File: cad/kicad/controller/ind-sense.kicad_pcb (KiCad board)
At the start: 2 copper layers, 32.5 x 81.2 mm, 21 parts, among them J1 Conn_01x27, J2 Conn_01x18, U1 74HC154, U2 MCP4821, U3 CMP04, U4 CMP04

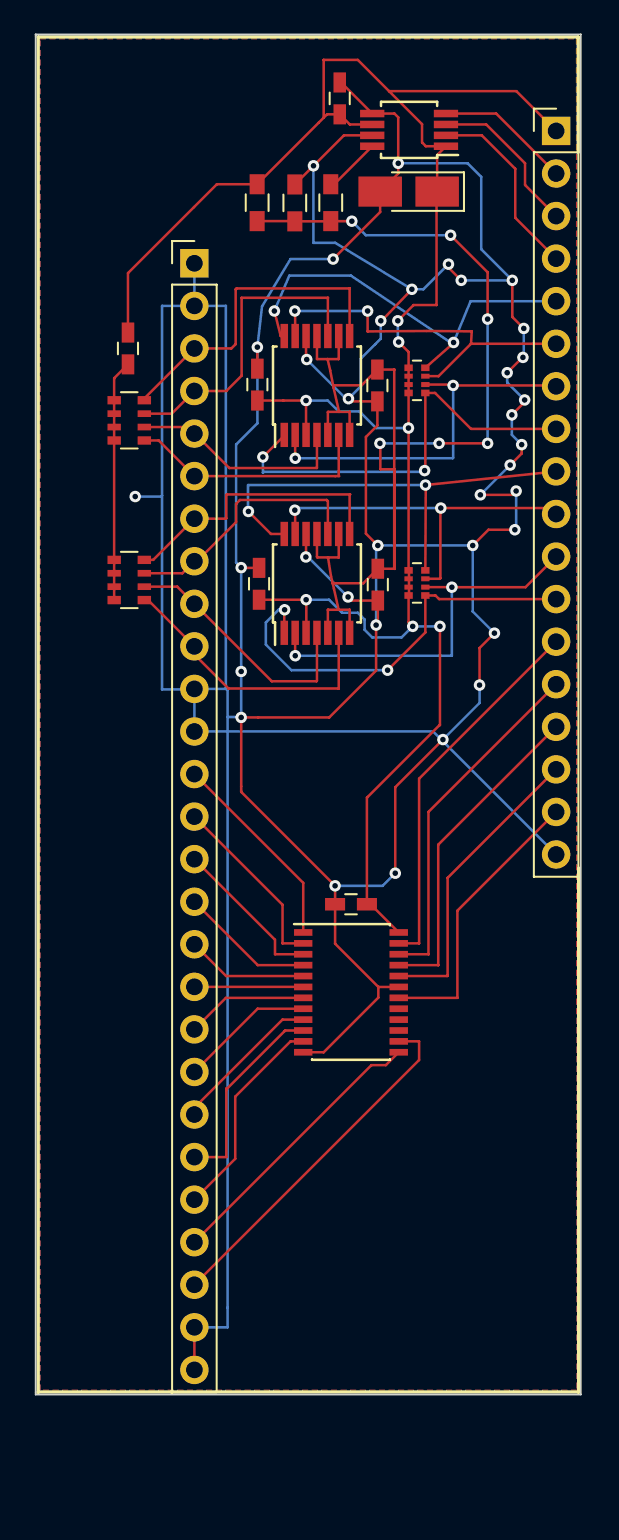
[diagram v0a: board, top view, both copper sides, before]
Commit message: updated controller with a lower part count equivalent, that should also be more accurate. need to have an actuall EE review the board and it's design
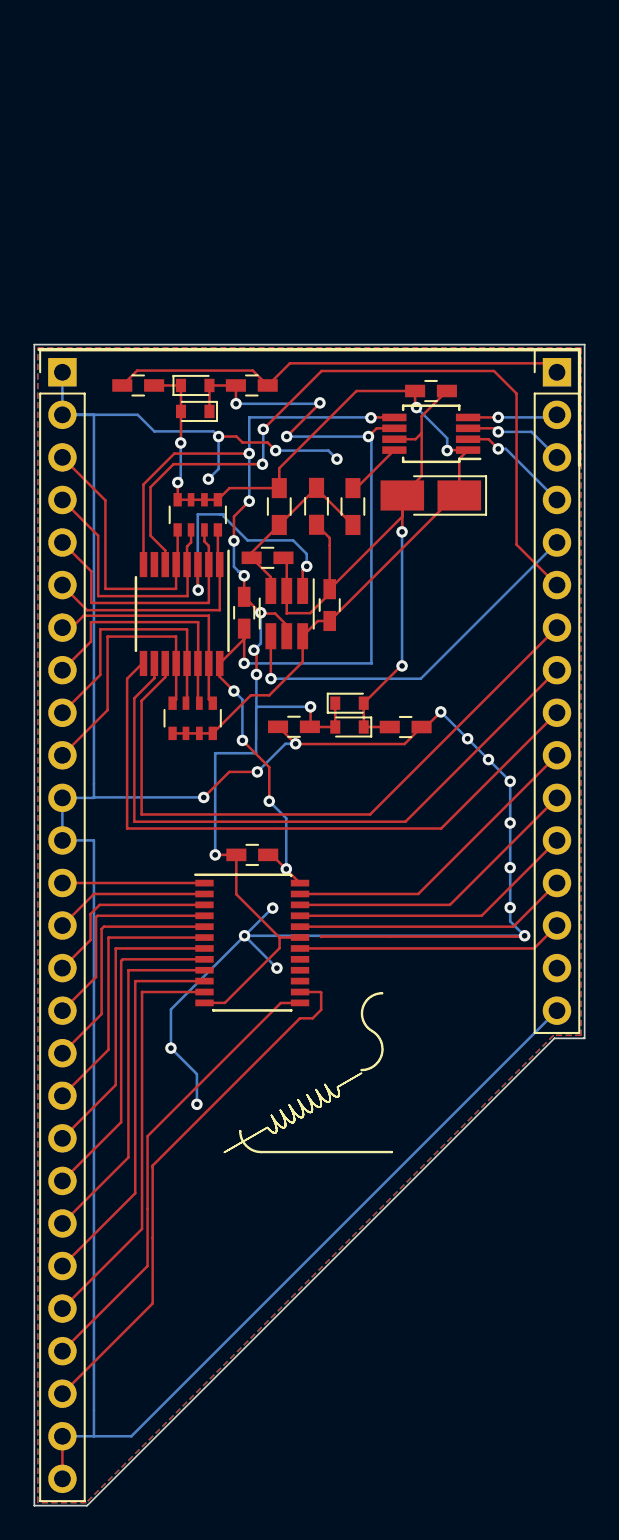
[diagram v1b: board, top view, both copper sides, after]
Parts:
- removed RN3, RN4: 66k, Resistors_SMD:R_Array_Convex_4x0402
- added C10: 0u1, Capacitors_SMD:C_0603_HandSoldering, F.Cu at (163.3, 56.5)
- added C9: 0u1, Capacitors_SMD:C_0603_HandSoldering, F.Cu at (156.6, 56.5)
- added D1: ~, Diodes_SMD:D_0603, F.Cu at (169.2, 76.8)
- added D2: ~, Diodes_SMD:D_0603, F.Cu at (169.2, 75.4)
- added D3: ~, Diodes_SMD:D_0603, F.Cu at (160.0, 56.5)
- added D4: ~, Diodes_SMD:D_0603, F.Cu at (160.0, 58.0)
- C2: value 100u -> 0u1
- J2: value Conn_01x18 -> Conn_01x16; footprint Pin_Headers:Pin_Header_Straight_1x18_Pitch2.54mm -> Pin_Headers:Pin_Header_Straight_1x16_Pitch2.54mm
- RN1, RN2: value 330 -> 2k64
- U3: value CMP04 -> NX3L4051; footprint Housings_SSOP:TSSOP-14_4.4x5mm_Pitch0.65mm -> Housings_SSOP:TSSOP-16_4.4x5mm_Pitch0.65mm
- U4: value CMP04 -> LMV761; footprint Housings_SSOP:TSSOP-14_4.4x5mm_Pitch0.65mm -> TO_SOT_Packages_SMD:SOT-23-6_Handsoldering
- moved C2 28.0 mm to (172.5, 76.8), turned to 0 degrees
- moved C3 18.3 mm to (174.0, 56.8), turned to 0 degrees
- moved C4 18.2 mm to (174.0, 63.0)
- moved R1 18.2 mm to (169.4, 63.7)
- moved R2 18.2 mm to (165.0, 63.7)
- moved U2 18.2 mm to (174.1, 59.3)
- moved R3 18.2 mm to (167.2, 63.7), turned to 270 degrees
- moved U3 15.9 mm to (159.2, 70.1), turned to 270 degrees
- moved C5 15.7 mm to (162.9, 70.0), turned to 90 degrees
- moved J2 14.4 mm to (181.6, 55.7)
- moved C6 10.4 mm to (164.3, 66.8), turned to 0 degrees
- moved J1 10.2 mm to (152.0, 55.7)
- moved RN2 9.08 mm to (159.8, 76.3), turned to 270 degrees
- moved C8 8.78 mm to (165.9, 76.8), turned to 180 degrees
- moved RN1 6.97 mm to (160.1, 64.2), turned to 270 degrees
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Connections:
- C2 pad 1: +3V3 -> GNDA
- C2 pad 2: Net-(C2-Pad2) -> GNDREF
- C3 pad 1: +3V3 -> +3.3VA
- C3 pad 2: GND -> GNDA
- C4 pad 1: +3V3 -> +3.3VA
- C4 pad 2: GND -> GNDA
- C5 pad 1: SP -> +3V3
- C6 pad 1: +3V3 -> Net-(C6-Pad1)
- C6 pad 2: GND -> GNDA
- C7 pad 1: SP -> +3.3VA
- C7 pad 2: GND -> GNDA
- C8 pad 1: +3V3 -> GND
- C8 pad 2: GND -> GNDREF
- J1 pad 1: GND -> GNDREF
- J1 pad 11: GND -> GNDREF
- J1 pad 12: GND -> GNDREF
- J1 pad 2: GND -> GNDREF
- J1 pad 26: GND -> GNDREF
- J1 pad 27: GND -> GNDREF
- J2 pad 1: +3V3 -> +3.3VP
- J2 pad 10: S6 -> CSEL1
- J2 pad 11: S7 -> CSEL2
- J2 pad 12: S8 -> CSEL3
- J2 pad 13: SEL1 -> CSEL4
- J2 pad 14: SEL2 -> ~CSTROBE
- J2 pad 15: SEL3 -> (no net)
- J2 pad 16: SEL4 -> GNDREF
- J2 pad 5: S1 -> OUT
- J2 pad 6: S2 -> ~RSTROBE
- J2 pad 7: S3 -> RSEL1
- J2 pad 8: S4 -> RSEL2
- J2 pad 9: S5 -> RSEL3
- R1 pad 2: SP -> Net-(C6-Pad1)
- R2 pad 1: +3V3 -> +3.3VA
- R2 pad 2: SP -> Net-(C6-Pad1)
- R3 pad 1: SP -> Net-(C6-Pad1)
- R3 pad 2: GND -> GNDA
- RN1 pad 1: M4 -> +3.3VA
- RN1 pad 2: M3 -> +3.3VA
- RN1 pad 3: M2 -> +3.3VA
- RN1 pad 4: M1 -> +3.3VA
- RN1 pad 5: Net-(C2-Pad2) -> M1
- RN1 pad 6: Net-(C2-Pad2) -> M2
- RN1 pad 7: Net-(C2-Pad2) -> M3
- RN1 pad 8: Net-(C2-Pad2) -> M4
- RN2 pad 1: M8 -> M5
- RN2 pad 2: M7 -> M6
- RN2 pad 3: M6 -> M7
- RN2 pad 4: M5 -> M8
- RN2 pad 5: Net-(C2-Pad2) -> +3.3VA
- RN2 pad 6: Net-(C2-Pad2) -> +3.3VA
- RN2 pad 7: Net-(C2-Pad2) -> +3.3VA
- RN2 pad 8: Net-(C2-Pad2) -> +3.3VA
- U1 pad 18: ~STROBE -> ~CSTROBE
- U1 pad 20: SEL4 -> CSEL4
- U1 pad 21: SEL3 -> CSEL3
- U1 pad 22: SEL2 -> CSEL2
- U1 pad 23: SEL1 -> CSEL1
- U2 pad 1: +3V3 -> +3.3VA
- U2 pad 7: GND -> GNDA
- U3 pad 1: S4 -> M4
- U3 pad 10: M2 -> RSEL2
- U3 pad 11: SP -> RSEL1
- U3 pad 12: GND -> M8
- U3 pad 13: S2 -> M7
- U3 pad 14: S1 -> M6
- U3 pad 2: S3 -> M3
- U3 pad 3: +3V3 -> Net-(U3-Pad3)
- U3 pad 4: M3 -> M2
- U3 pad 5: SP -> M1
- U3 pad 6: M4 -> ~RSTROBE
- U3 pad 7: SP -> (no net)
- U3 pad 8: M1 -> GND
- U3 pad 9: SP -> RSEL3
- U4 pad 1: S8 -> Net-(U3-Pad3)
- U4 pad 2: S7 -> GNDA
- U4 pad 3: +3V3 -> Net-(C6-Pad1)
- U4 pad 4: M7 -> OUT
- U4 pad 5: SP -> GND
- U4 pad 6: M8 -> +3.3VA
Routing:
- net GND: track 345.0 -> 75.4 mm, vias 35 -> 10
- net GNDREF: track 0.00 -> 218.2 mm, vias 0 -> 20
- net SP: track 82.9 -> 0.00 mm, vias 6 -> 0
- net +3V3: track 125.0 -> 61.3 mm, vias 7 -> 9
- net +3.3VA: track 0.00 -> 60.9 mm, vias 0 -> 4
- net GNDA: track 0.00 -> 44.9 mm, vias 0 -> 2
- net ~RSTROBE: track 0.00 -> 43.9 mm, vias 0 -> 2
- net RSEL1: track 0.00 -> 39.0 mm
- net RSEL2: track 0.00 -> 38.9 mm
- net RSEL3: track 0.00 -> 38.8 mm
- net S5: track 27.8 -> 0.00 mm, vias 2 -> 0
- net +3.3VP: track 0.00 -> 27.7 mm
- net S4: track 25.9 -> 0.00 mm, vias 2 -> 0
- net S8: track 25.3 -> 0.00 mm, vias 2 -> 0
- net S1: track 25.1 -> 0.00 mm, vias 2 -> 0
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- added copper zone on B.Cu, net GNDREF
- added copper zone on F.Cu, net GNDREF
- removed copper zone on B.Cu, net GND
- removed copper zone on F.Cu, net GND
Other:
- board size 32.5 x 81.2 mm -> 32.8 x 69.3 mm
